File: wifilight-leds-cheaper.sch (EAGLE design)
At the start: 37 parts, among them Q1 BUK98180-100A, Q2 BUK98180-100A, Q3 BUK98180-100A, Q4 BUK98180-100A, U2 PCA9685

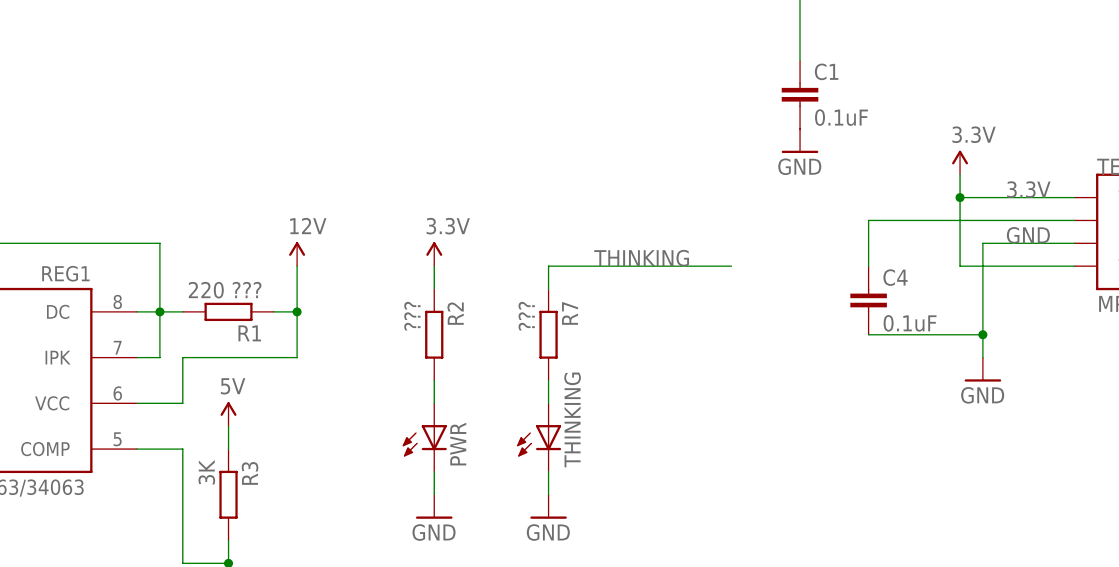
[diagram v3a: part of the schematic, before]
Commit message: adding resistor values and moved C4
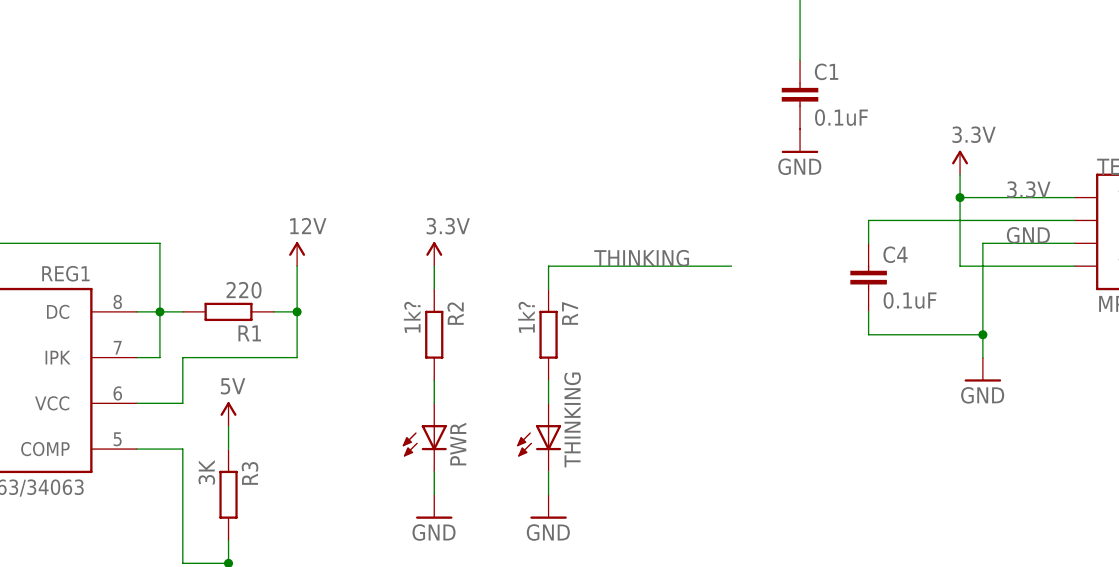
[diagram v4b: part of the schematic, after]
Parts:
- R1: value 220 ??? -> 220
- R2, R7: value ??? -> 1k?
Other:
- moved on the sheet: C4
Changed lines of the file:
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@@
 <part name="REG1" library="adafruit" deviceset="MC33063/MC34063" device="D"/>
 <part name="REG2" library="linear" deviceset="MC33269-SO8" device=""/>
-<part name="R1" library="resistor" deviceset="R-EU_" device="R0805" value="220 ???"/>
+<part name="R1" library="resistor" deviceset="R-EU_" device="R0805" value="220"/>
 <part name="PWR" library="led" deviceset="LED" device="CHIP-LED0805"/>
-<part name="R2" library="resistor" deviceset="R-EU_" device="R0805" value="???"/>
+<part name="R2" library="resistor" deviceset="R-EU_" device="R0805" value="1k?"/>
 <part name="SUPPLY10" library="SparkFun-Aesthetics" deviceset="3.3V" device=""/>
 <part name="GND6" library="supply1" deviceset="GND" device=""/>
@@
 <part name="SUPPLY17" library="SparkFun-Aesthetics" deviceset="3.3V" device=""/>
 <part name="THINKING" library="led" deviceset="LED" device="CHIP-LED0805"/>
-<part name="R7" library="resistor" deviceset="R-EU_" device="R0805" value="???"/>
+<part name="R7" library="resistor" deviceset="R-EU_" device="R0805" value="1k?"/>
 <part name="GND16" library="supply1" deviceset="GND" device=""/>
 <part name="A" library="adafruit" deviceset="PINHD-1X1" device=""/>
@@
 <instance part="SUPPLY15" gate="G$1" x="63.5" y="132.08"/>
 <instance part="GND10" gate="1" x="66.04" y="109.22"/>
-<instance part="C4" gate="G$1" x="53.34" y="119.38"/>
+<instance part="C4" gate="G$1" x="53.34" y="121.92"/>
 <instance part="SUPPLY16" gate="G$1" x="45.72" y="152.4"/>
 <instance part="SUPPLY17" gate="G$1" x="17.78" y="175.26"/>
@@
 <pinref part="C4" gate="G$1" pin="2"/>
 <wire x1="66.04" y1="114.3" x2="66.04" y2="111.76" width="0.1524" layer="91"/>
+<wire x1="53.34" y1="116.84" x2="53.34" y2="114.3" width="0.1524" layer="91"/>
 <wire x1="53.34" y1="114.3" x2="66.04" y2="114.3" width="0.1524" layer="91"/>
 <junction x="66.04" y="114.3"/>
@@
 <wire x1="76.2" y1="127" x2="53.34" y2="127" width="0.1524" layer="91"/>
 <pinref part="C4" gate="G$1" pin="1"/>
-<wire x1="53.34" y1="127" x2="53.34" y2="121.92" width="0.1524" layer="91"/>
-</segment>
-</net>
+<wire x1="53.34" y1="127" x2="53.34" y2="124.46" width="0.1524" layer="91"/>
+</segment>
+</net>
